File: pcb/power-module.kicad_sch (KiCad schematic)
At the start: 49 parts, among them J2 USB_C_PowerOnly_6P, J3 Power, U1 LD1117S33TR_SOT223, U2 FDS4435BZ, U3 FDS4435BZ

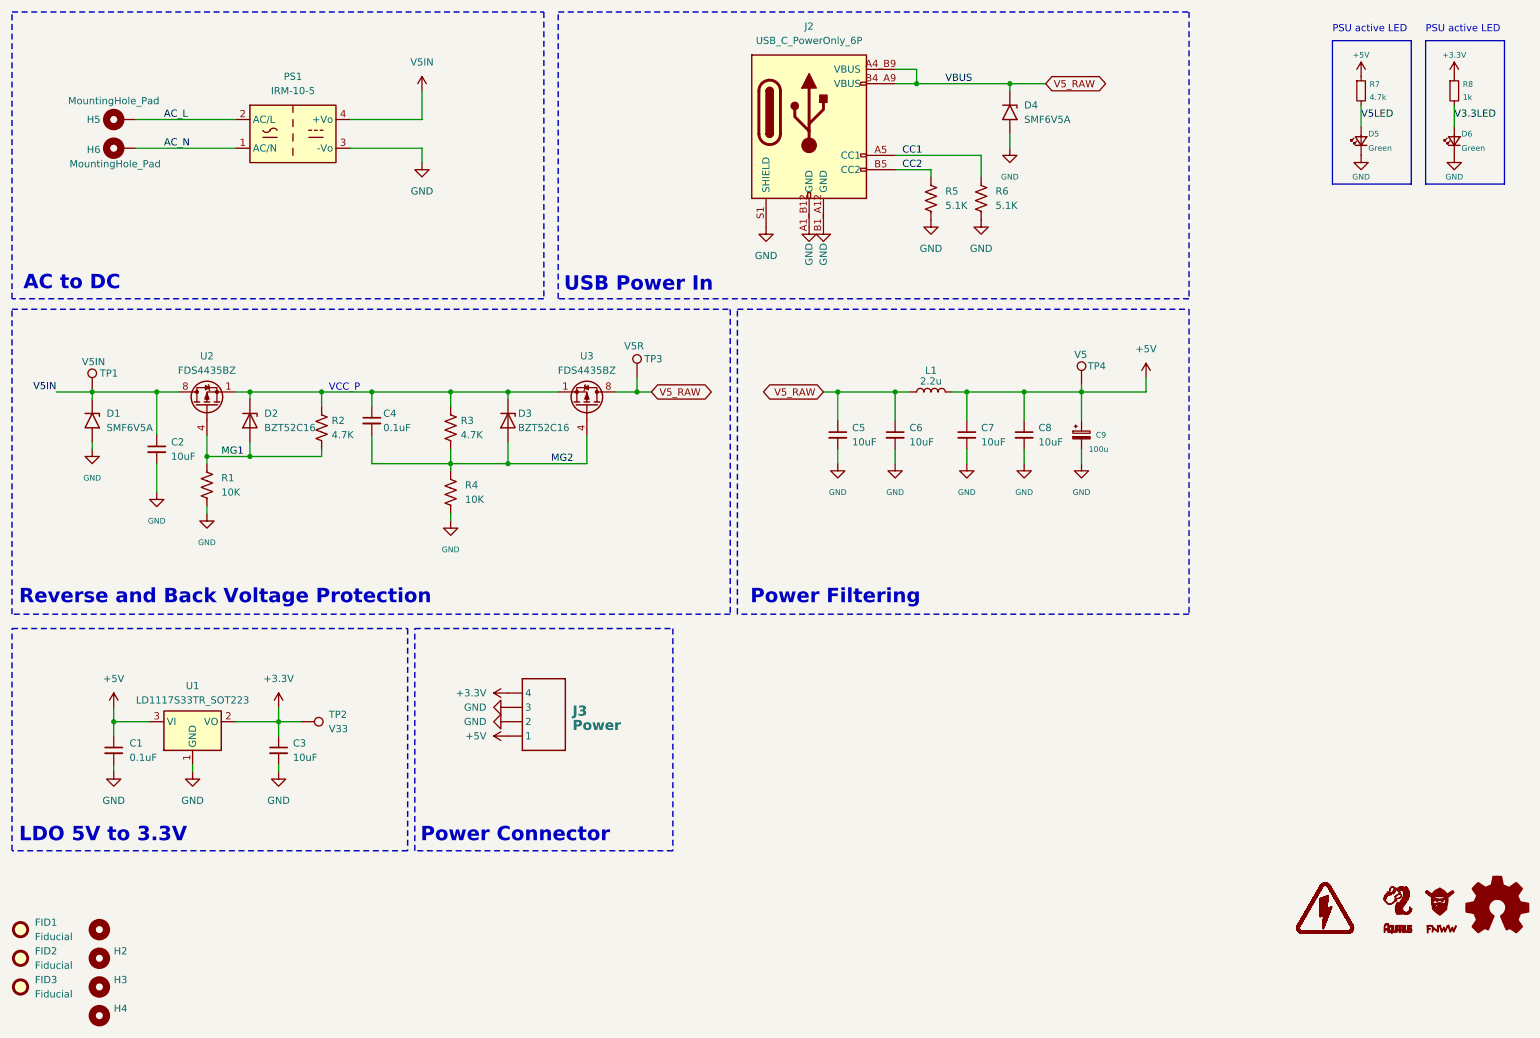
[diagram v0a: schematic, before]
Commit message: Updated foot prints; maybe deprecated
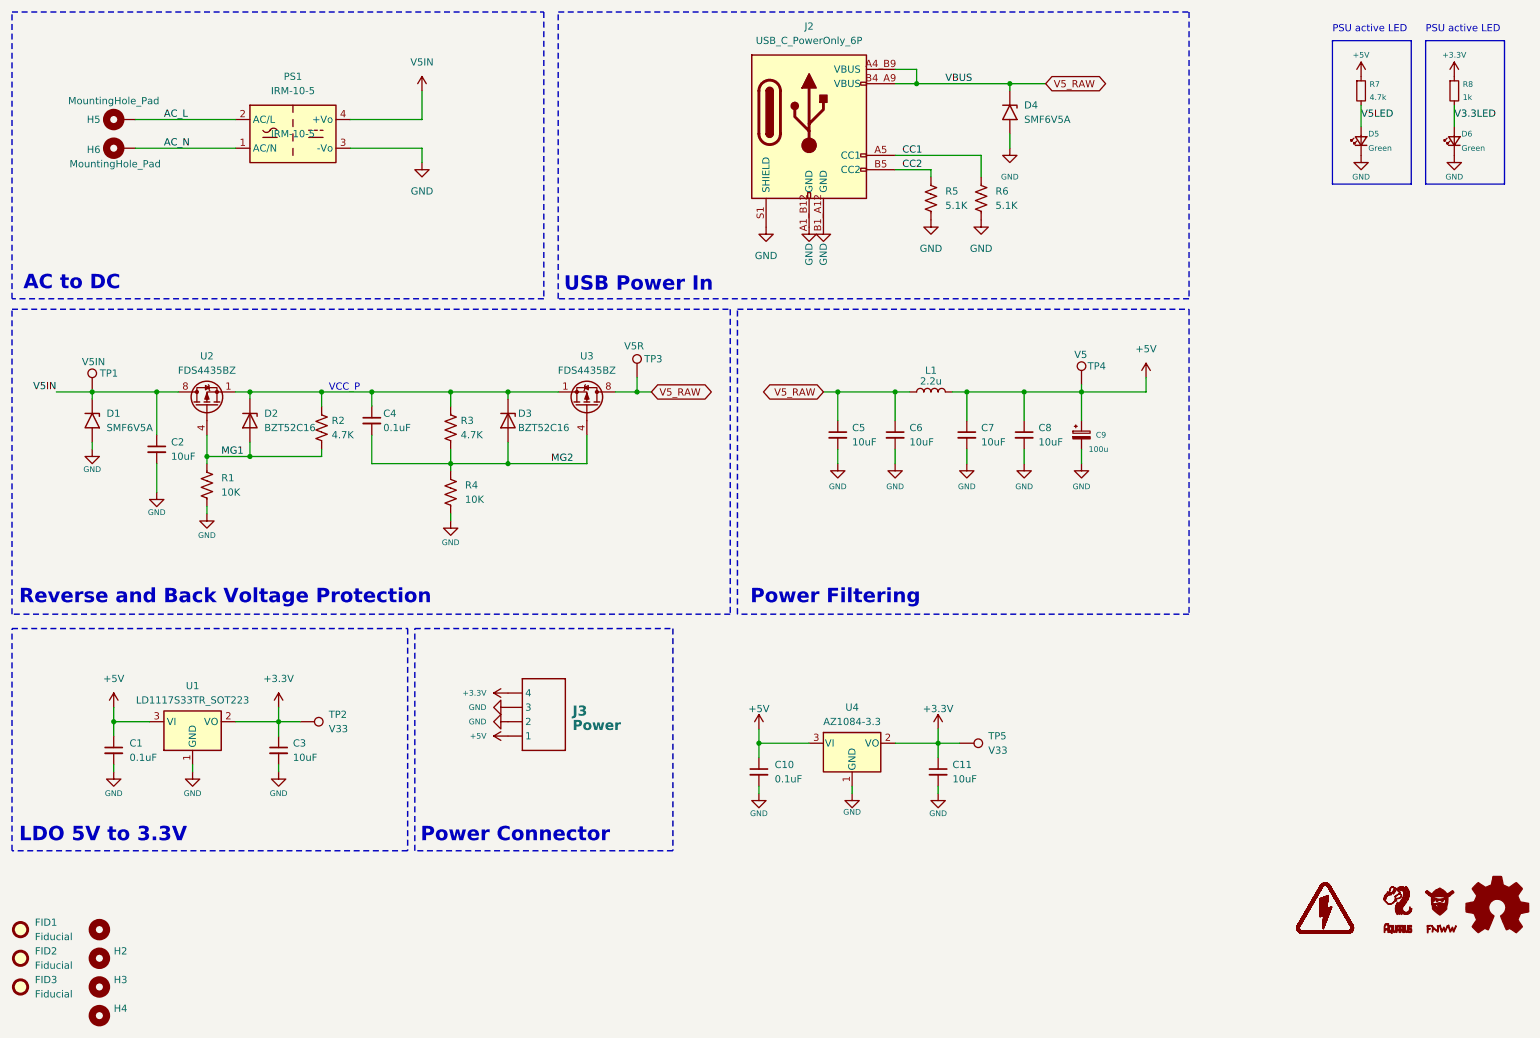
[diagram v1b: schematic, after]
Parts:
- added C10: 0.1uF, Capacitor_SMD:C_0603_1608Metric, symbol Device:C_Small
- added C11: 10uF, Capacitor_SMD:C_0603_1608Metric, symbol Device:C_Small
- added TP5: V33, TestPoint:TestPoint_Pad_D1.0mm, symbol Connector:TestPoint
- added U4: AZ1084-3.3, Package_TO_SOT_SMD:TO-252-2, symbol Regulator_Linear:AZ1084-3.3
- J2: LCSC (none) -> C165948
- PS1: MPN (none) -> IRM-10-5
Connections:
- net +3.3V: now also C11.1, TP5.1, U4.2 (VO)
- net +5V: now also C10.1, U4.3 (VI)
- net GND: now also C10.2, C11.2, U4.1 (GND)
